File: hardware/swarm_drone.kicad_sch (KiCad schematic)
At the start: 0 parts

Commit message: feat(hardware): add STM32F405 core power, decoupling, reset, and boot schematic
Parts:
- added C1, C10, C2, C3, C4, C5: 100n, symbol Device:C
- added C6: 10u, symbol Device:C
- added C7: 10n, symbol Device:C
- added C8, C9: 1u, symbol Device:C
- added FB1: 120R, symbol Device:FerriteBead
- added R1, R2: 10k, symbol Device:R
- added SW1: SW_Push, symbol Switch:SW_Push
- added U1: STM32F405RGT7, Package_QFP:LQFP-64_10x10mm_P0.5mm, symbol MCU_ST_STM32F4:STM32F405RGTx
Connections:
- new net +3V3: C1.1, C2.1, C3.1, C4.1, C5.1, C6.1, C7.1, C8.1, C9.1, FB1.1, FB1.2, R2.2, U1.1 (VBAT), U1.13 (VDDA), U1.19 (VDD), U1.32 (VDD), U1.48 (VDD), U1.64 (VDD)
- new net BOOT0: R1.2, U1.60 (BOOT0)
- new net GND: C1.2, C10.2, C2.2, C3.2, C4.2, C5.2, C6.2, C7.2, C8.2, C9.2, R1.1, SW1.1, U1.12 (VSSA), U1.18 (VSS), U1.63 (VSS)
- new net NRST: C10.1, R2.1, SW1.2, U1.7 (NRST)
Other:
- note added: "MCU"

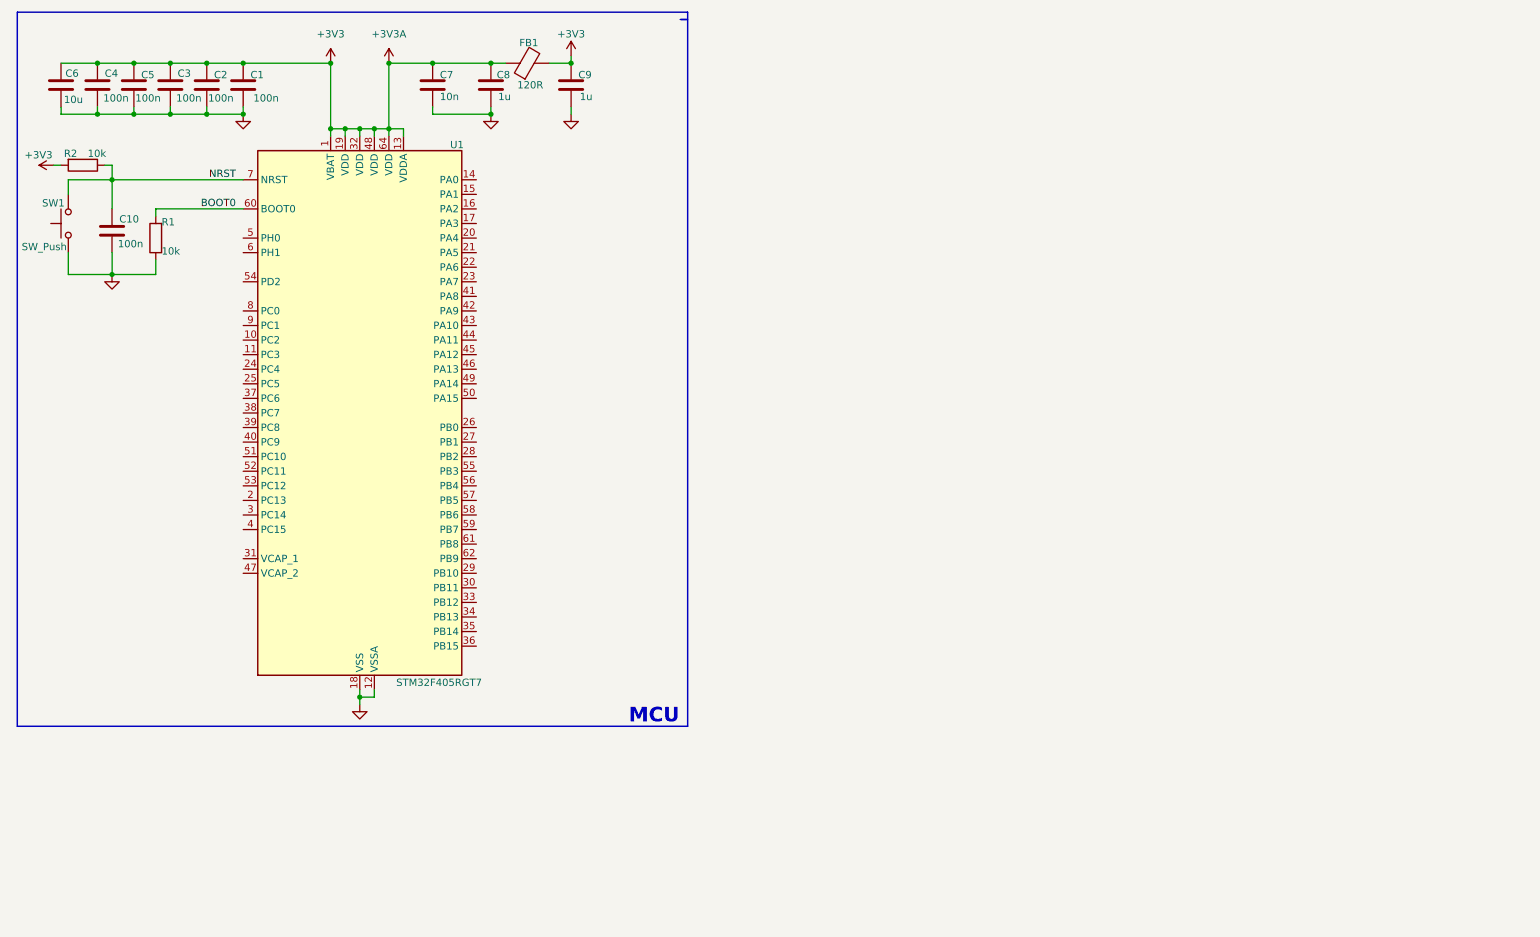
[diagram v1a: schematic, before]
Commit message: feat(kicad): Added MCU schematic and LDO schematic
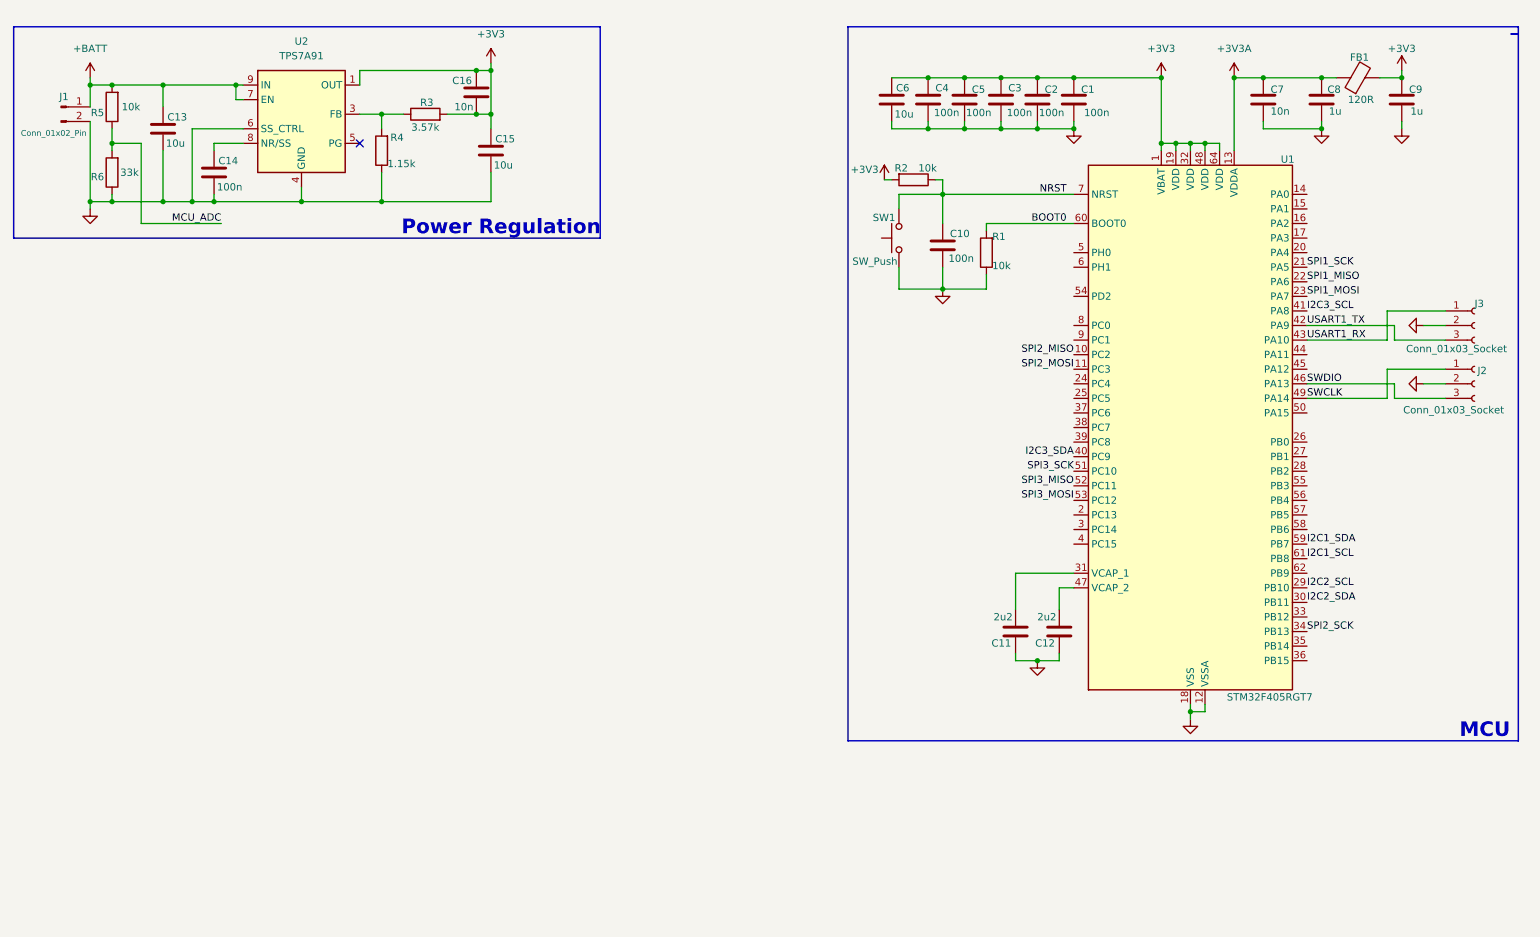
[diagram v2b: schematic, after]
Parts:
- added C11, C12: 2u2, Capacitor_SMD:C_0402_1005Metric, symbol Device:C
- added C13, C15: 10u, Capacitor_SMD:C_0603_1608Metric, symbol Device:C
- added C14: 100n, Capacitor_SMD:C_0402_1005Metric, symbol Device:C
- added C16: 10n, Capacitor_SMD:C_0402_1005Metric, symbol Device:C
- added J1: Conn_01x02_Pin, Connector_JST:JST_PH_S2B-PH-K_1x02_P2.00mm_Horizontal, symbol Connector:Conn_01x02_Pin
- added J2, J3: Conn_01x03_Socket, Connector_PinHeader_1.00mm:PinHeader_1x03_P1.00mm_Horizontal, symbol Connector:Conn_01x03_Socket
- added R3: 3.57k, Resistor_SMD:R_0402_1005Metric, symbol Device:R
- added R4: 1.15k, Resistor_SMD:R_0402_1005Metric, symbol Device:R
- added R5: 10k, Resistor_SMD:R_0402_1005Metric, symbol Device:R
- added R6: 33k, Resistor_SMD:R_0402_1005Metric, symbol Device:R
- added U2: TPS7A91, Package_DFN_QFN:Texas_S-PDSO-N10_EP1.2x2mm, symbol Regulator_Linear:TPS7A91
- C1, C10, C2, C3, C4, C5, C7, C8, C9: footprint (none) -> Capacitor_SMD:C_0402_1005Metric
- C6: footprint (none) -> Capacitor_SMD:C_0603_1608Metric
- FB1: footprint (none) -> Inductor_SMD:L_0603_1608Metric
- R1, R2: footprint (none) -> Resistor_SMD:R_0402_1005Metric
- SW1: footprint (none) -> Button_Switch_SMD:SW_Push_1P1T_NO_CK_KSC6xxG
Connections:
- net +3V3: now also C15.1, C16.1, C16.2, R3.2, U2.1 (OUT), U2.2 (OUT); no longer C7.1, C8.1, FB1.1, U1.13 (VDDA)
- net GND: now also C11.1, C12.1, C13.2, C14.2, C15.2, J1.2 (Pin_2), J2.2 (Pin_2), J3.2 (Pin_2), R4.1, R6.1, U2.11 (GND), U2.4 (GND), U2.6 (SS_CTRL)
- net SPI2_MISO: now reaches U1.10 (PC2)
- net SPI2_MOSI: now reaches U1.11 (PC3)
- net SPI1_SCK: now reaches U1.21 (PA5)
- net SPI1_MISO: now reaches U1.22 (PA6)
- net SPI1_MOSI: now reaches U1.23 (PA7)
- net I2C2_SCL: now reaches U1.29 (PB10)
- net I2C2_SDA: now reaches U1.30 (PB11)
- net at U1.31 (VCAP_1): now also C11.2
- net SPI2_SCK: now reaches U1.34 (PB13)
- net I2C3_SDA: now reaches U1.40 (PC9)
- net I2C3_SCL: now reaches U1.41 (PA8)
- net USART1_TX: now reaches U1.42 (PA9)
- net USART1_TX: now also J3.3 (Pin_3)
- net USART1_RX: now reaches U1.43 (PA10)
- net USART1_RX: now also J3.1 (Pin_1)
- net SWDIO: now reaches U1.46 (PA13)
- net SWDIO: now also J2.3 (Pin_3)
- net at U1.47 (VCAP_2): now also C12.2
- net SWCLK: now reaches U1.49 (PA14)
- net SWCLK: now also J2.1 (Pin_1)
- net SPI3_SCK: now reaches U1.51 (PC10)
- net SPI3_MISO: now reaches U1.52 (PC11)
- net SPI3_MOSI: now reaches U1.53 (PC12)
- net I2C1_SDA: now reaches U1.59 (PB7)
- net I2C1_SCL: now reaches U1.61 (PB8)
- new net: R3.1, R4.2, U2.3 (FB)
- new net: C14.1, U2.8 (NR/SS)
- new net: R5.1, R6.2
- new net +3V3A: C7.1, C8.1, FB1.1, U1.13 (VDDA)
- new net +BATT: C13.1, J1.1 (Pin_1), R5.2, U2.10 (IN), U2.7 (EN), U2.9 (IN)
- no-connect marks 0 -> 1
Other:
- note added: "Power Regulation"
- moved on the sheet: C1, C10, C2, C3, C4, C5, C6, C7, C8, C9, FB1, R1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

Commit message: feat: Added schematic design for IMU and Barometer. Included reference sheets and open sourcer models
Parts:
- added C17: 0.1u, Capacitor_SMD:C_0603_1608Metric, symbol Device:C
- added C18: 2.2u, Capacitor_SMD:C_0603_1608Metric, symbol Device:C
- added C19: 10n, Capacitor_SMD:C_0603_1608Metric, symbol Device:C
- added R7: 10k, Resistor_SMD:R_0402_1005Metric, symbol Device:R
- added U3: ICM-42688-P, ICM-42688-P:PQFN50P300X250X97-14N, symbol ICM-42688-P:ICM-42688-P
- added U4: BMP581, QFN10_BMP581_BOS, symbol 2026-10-13_02-17-36:BMP581
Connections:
- net +3V3: now also C17.1, C18.1, C19.1, R7.2, U3.5 (VDDIO), U3.8 (VDD)
- net GND: now also C17.2, C18.2, C19.2, U3.10 (RESV_10), U3.11 (RESV_11), U3.2 (RESV_2), U3.3 (RESV_3), U3.6 (GND), U3.7 (RESV_7), U3.9 (INT2/FSYNC/CLKIN)
- net SPI1_MISO: now also U3.1 (AP_SDO/AP_AD0)
- net SPI1_MOSI: now also U3.14 (AP_SDA/AP_SDIO/AP_SDI)
- net SPI1_SCK: now also U3.13 (AP_SCL/AP_SCLK)
- new net IMU_CS: R7.1, U3.12 (AP_CS)
- new net IMU_INT: U3.4 (INT1/INT)
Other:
- note added: "Barometer"
- note added: "IMU"

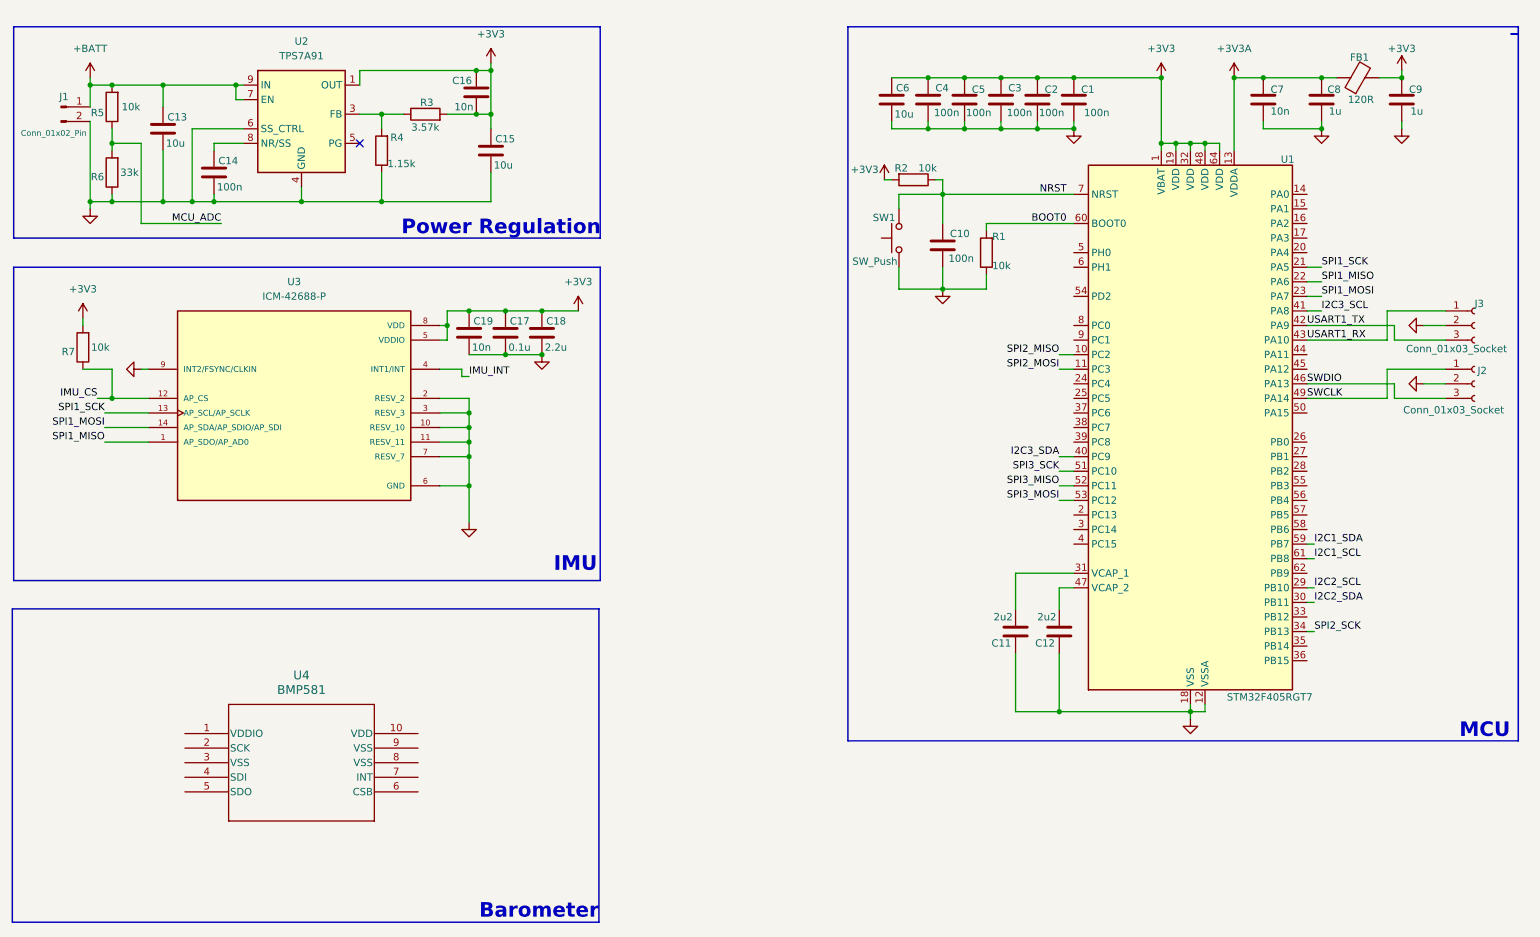
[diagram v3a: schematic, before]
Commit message: feat(kicad): Added heirarchical subsheets and block diagrams to indicate system behavior
Added barometer schematic
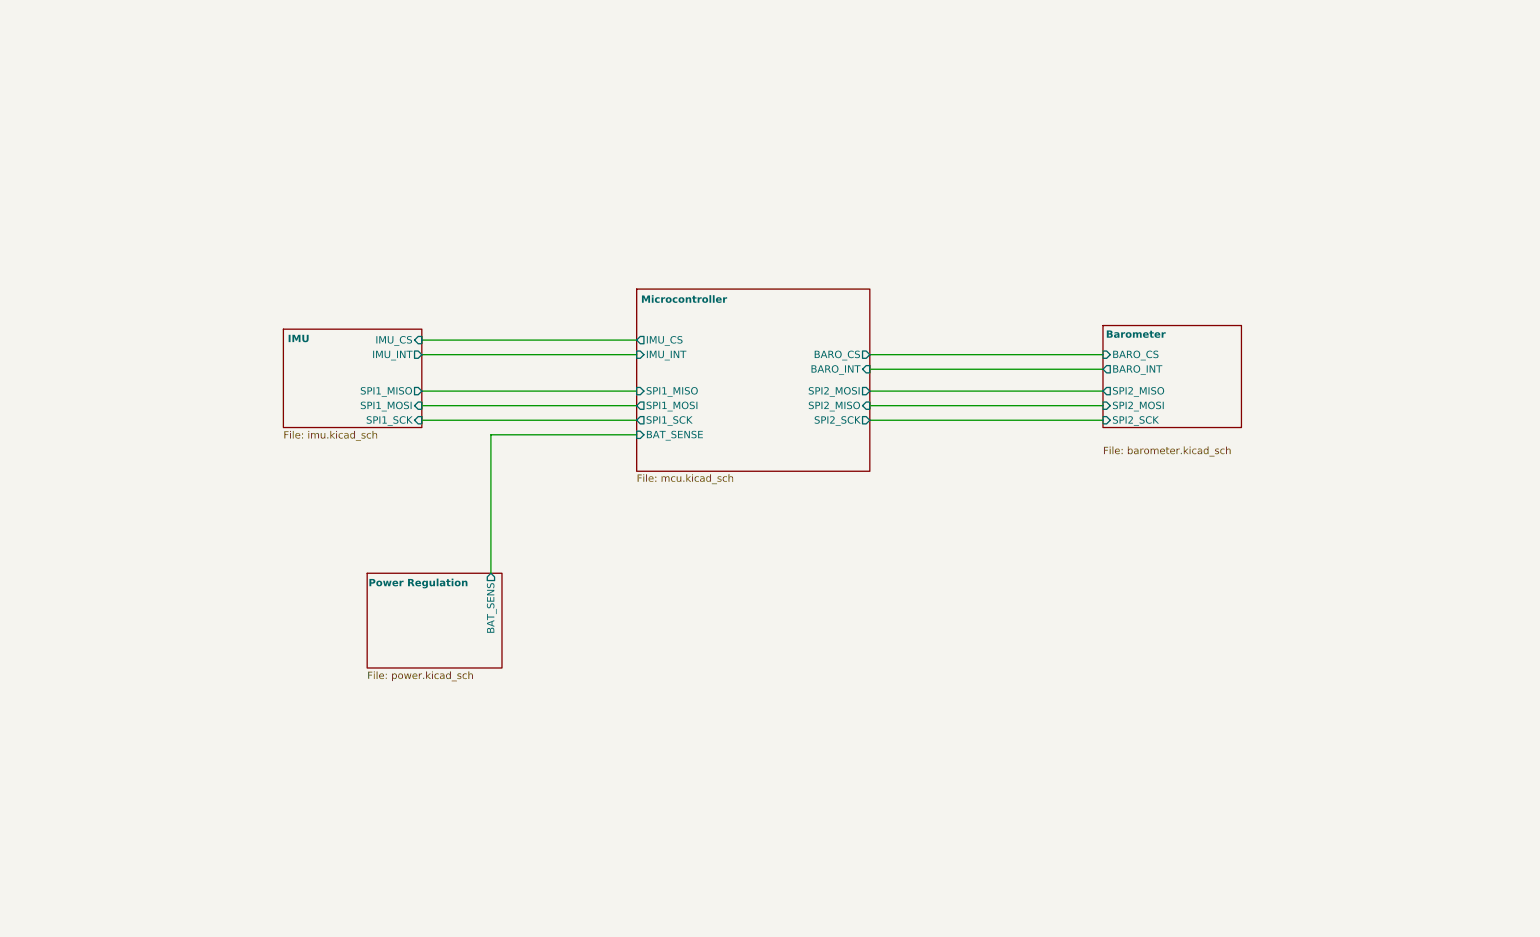
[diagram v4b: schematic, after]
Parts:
- removed C1, C10, C14, C2, C3, C4, C5: 100n, Capacitor_SMD:C_0402_1005Metric, symbol Device:C
- removed C11, C12: 2u2, Capacitor_SMD:C_0402_1005Metric, symbol Device:C
- removed C13, C15, C6: 10u, Capacitor_SMD:C_0603_1608Metric, symbol Device:C
- removed C16, C7: 10n, Capacitor_SMD:C_0402_1005Metric, symbol Device:C
- removed C17: 0.1u, Capacitor_SMD:C_0603_1608Metric, symbol Device:C
- removed C18: 2.2u, Capacitor_SMD:C_0603_1608Metric, symbol Device:C
- removed C19: 10n, Capacitor_SMD:C_0603_1608Metric, symbol Device:C
- removed C8, C9: 1u, Capacitor_SMD:C_0402_1005Metric, symbol Device:C
- removed FB1: 120R, Inductor_SMD:L_0603_1608Metric, symbol Device:FerriteBead
- removed J1: Conn_01x02_Pin, Connector_JST:JST_PH_S2B-PH-K_1x02_P2.00mm_Horizontal, symbol Connector:Conn_01x02_Pin
- removed J2, J3: Conn_01x03_Socket, Connector_PinHeader_1.00mm:PinHeader_1x03_P1.00mm_Horizontal, symbol Connector:Conn_01x03_Socket
- removed R1, R2, R5, R7: 10k, Resistor_SMD:R_0402_1005Metric, symbol Device:R
- removed R3: 3.57k, Resistor_SMD:R_0402_1005Metric, symbol Device:R
- removed R4: 1.15k, Resistor_SMD:R_0402_1005Metric, symbol Device:R
- removed R6: 33k, Resistor_SMD:R_0402_1005Metric, symbol Device:R
- removed SW1: SW_Push, Button_Switch_SMD:SW_Push_1P1T_NO_CK_KSC6xxG, symbol Switch:SW_Push
- removed U1: STM32F405RGT7, Package_QFP:LQFP-64_10x10mm_P0.5mm, symbol MCU_ST_STM32F4:STM32F405RGTx
- removed U2: TPS7A91, Package_DFN_QFN:Texas_S-PDSO-N10_EP1.2x2mm, symbol Regulator_Linear:TPS7A91
- removed U3: ICM-42688-P, ICM-42688-P:PQFN50P300X250X97-14N, symbol ICM-42688-P:ICM-42688-P
- removed U4: BMP581, QFN10_BMP581_BOS, symbol 2026-10-13_02-17-36:BMP581
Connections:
- no-connect marks 1 -> 0
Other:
- added sheet Barometer (barometer.kicad_sch)
- added sheet IMU (imu.kicad_sch)
- added sheet Microcontroller (mcu.kicad_sch)
- added sheet Power Regulation (power.kicad_sch)
- note removed: "Barometer"
- note removed: "IMU"
- note removed: "MCU"
- note removed: "Power Regulation"

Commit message: feat(kicad): Added heirarchical nodes for baro, imu. Added motor driving logic and updated pinouts
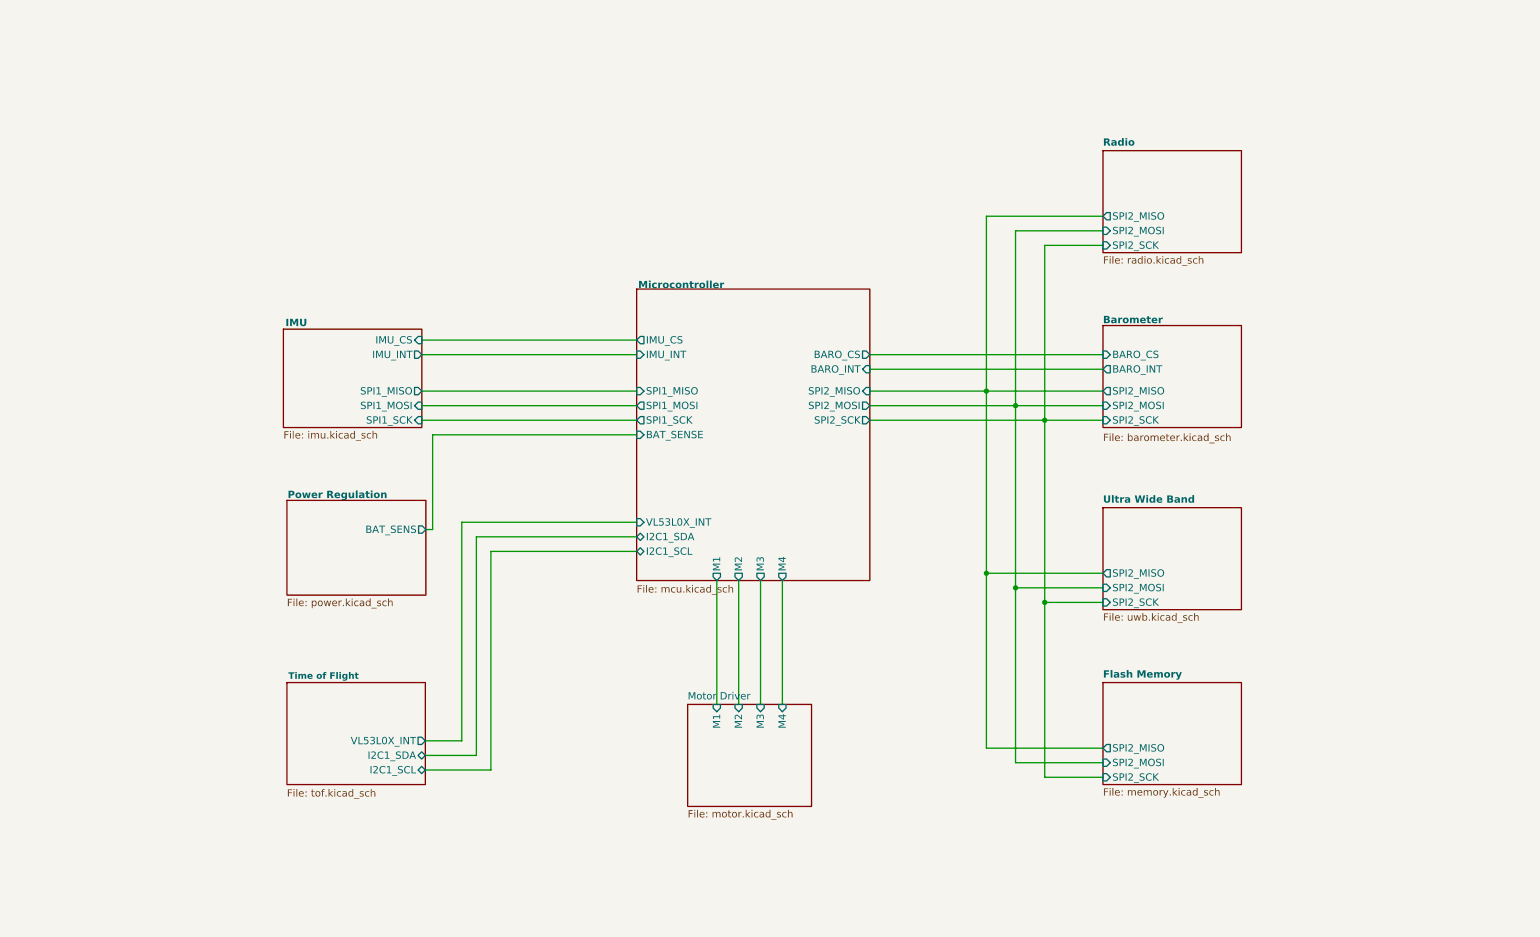
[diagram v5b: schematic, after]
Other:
- added sheet Flash Memory (memory.kicad_sch)
- added sheet Motor Driver (motor.kicad_sch)
- added sheet Radio (radio.kicad_sch)
- added sheet Time of Flight (tof.kicad_sch)
- added sheet Ultra Wide Band (uwb.kicad_sch)
- sheet Microcontroller ports: added I2C1_SCL, I2C1_SDA, M1, M2, M3, M4, VL53L0X_INT; removed none
